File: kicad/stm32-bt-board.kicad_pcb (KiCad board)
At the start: 4 copper layers, 55 x 35.2 mm, 54 parts, among them J1 1909763-1, J2 2171790001, J3 Conn_ARM_SWD_TagConnect_TC2030, J4 S4B-PH-K-S(LF)(SN), Q1 S9013-E, SW1 B3U-1000P, SW2 B3U-1000P, U1 MIC5365-3.3YD5, U2 USBLC6-2SC6, U3 USBLC6-2SC6, U4 STM32WB55CEU6, X1 32MHz, X2 32kHz768

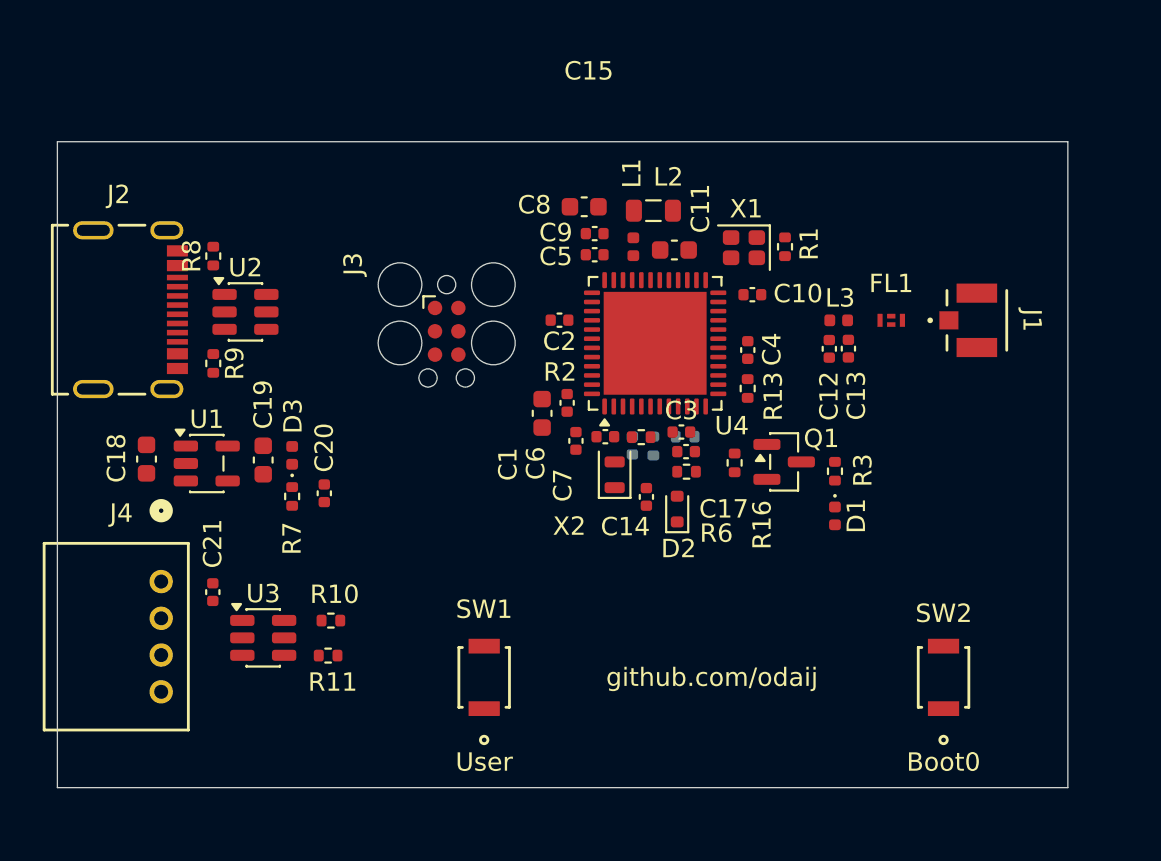
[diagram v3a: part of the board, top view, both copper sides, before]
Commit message: feat(layout & footprints): adjust layout and enhance custom footprints
adjust decoupling capacitors' positions and almost everything else
use rounded rectangular pads for all custom footprints, and update the pcb layout accordingly
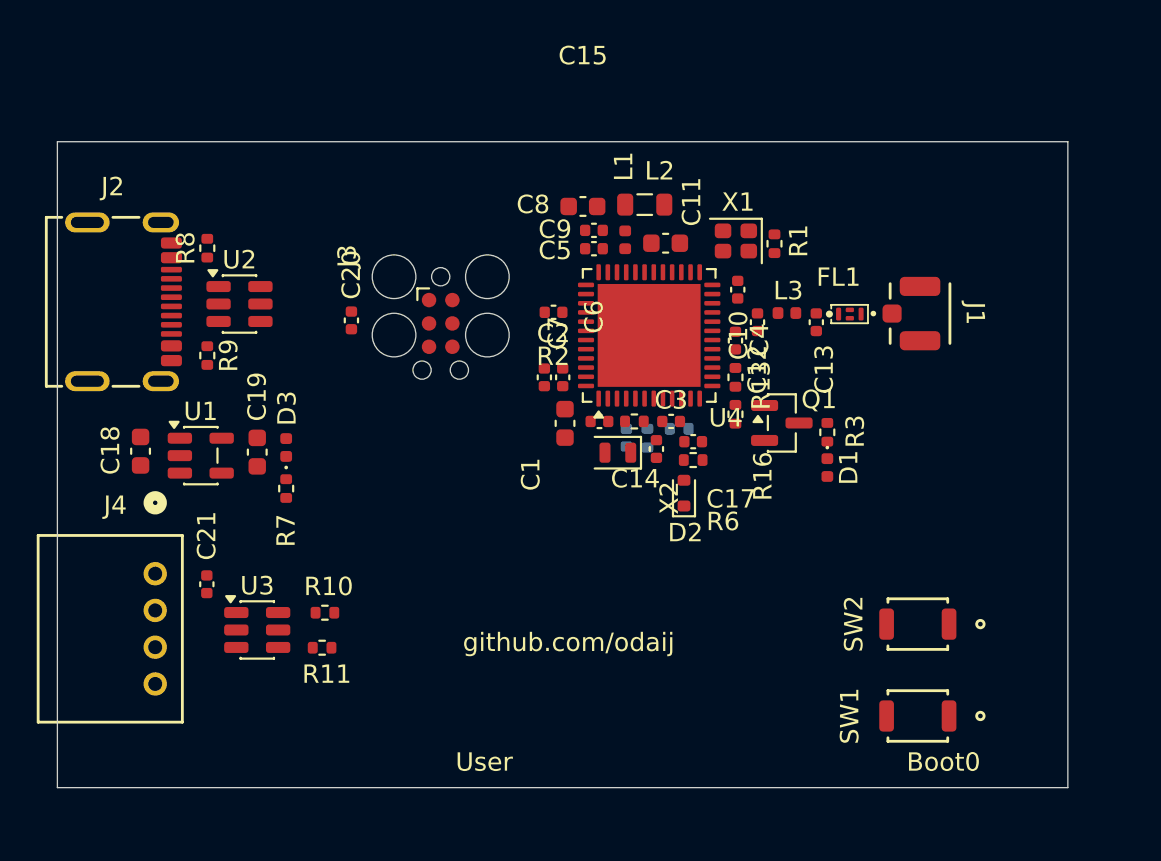
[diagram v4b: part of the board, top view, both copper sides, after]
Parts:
- moved SW1 23.7 mm to (169.0, 118.0), turned to 180 degrees
- moved C20 9.52 mm to (138.2, 96.5)
- moved C12 4.17 mm to (160.3, 96.6)
- moved C7 3.86 mm to (148.7, 99.6), turned to 90 degrees
- moved SW2 3.22 mm to (169.0, 113.0), turned to 180 degrees
- moved J1 3.11 mm to (169.1, 96.1)
- moved FL1 2.89 mm to (164.7, 96.1)
- moved L3 2.85 mm to (161.9, 96.1)
- moved C14 2.66 mm to (154.8, 103.5)
- moved D1 2.66 mm to (164.1, 104.5)
- moved R16 2.64 mm to (159.1, 101.6)
- moved C13 2.26 mm to (163.5, 96.6)
- moved R3 2.16 mm to (164.1, 102.6)
- moved Q1 2.12 mm to (161.6, 102.1)
- moved C6 1.41 mm to (149.7, 99.6), turned to 90 degrees
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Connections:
- net Net-(R1-Pad2) renamed /Microcontroller/Crystals/OSC_HSE_OUT_R

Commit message: i am in a hurry
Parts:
- moved C18 9.24 mm to (135.1, 99.7), turned to 180 degrees
- moved D3 5.75 mm to (135.6, 109.0), turned to 0 degrees
- moved R9 5.09 mm to (127.2, 102.4), turned to 180 degrees
- moved U1 5.07 mm to (134.9, 102.6), turned to -90 degrees
- moved R7 3.63 mm to (133.4, 109.0), turned to 180 degrees
- moved R8 3.49 mm to (127.2, 91.0), turned to 180 degrees
- moved U2 2.93 mm to (134.9, 96.4)
- moved C19 2.79 mm to (135.1, 105.5), turned to 180 degrees
- moved J2 2.12 mm to (126.8, 96.7)
- moved C14 1.13 mm to (154.7, 104.6)
- moved R1 1.03 mm to (162.1, 91.8)
- moved X1 1.03 mm to (160.0, 91.7)
- moved C16 0.97 mm to (154.1, 103.2)
- moved R5 0.88 mm to (155.1, 103.2)
- moved C15 0.73 mm to (151.6, 102.7)
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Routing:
- net /Microcontroller/BOOT0: track 0.00 -> 4.62 mm, vias 0 -> 1
- net /Microcontroller/OSC_LSE_IN: track 0.00 -> 3.76 mm
- net /Microcontroller/Crystals/OSC_LSE_OUT_R: track 0.00 -> 3.44 mm
- net /Microcontroller/OSC_LSE_OUT: track 0.00 -> 2.13 mm

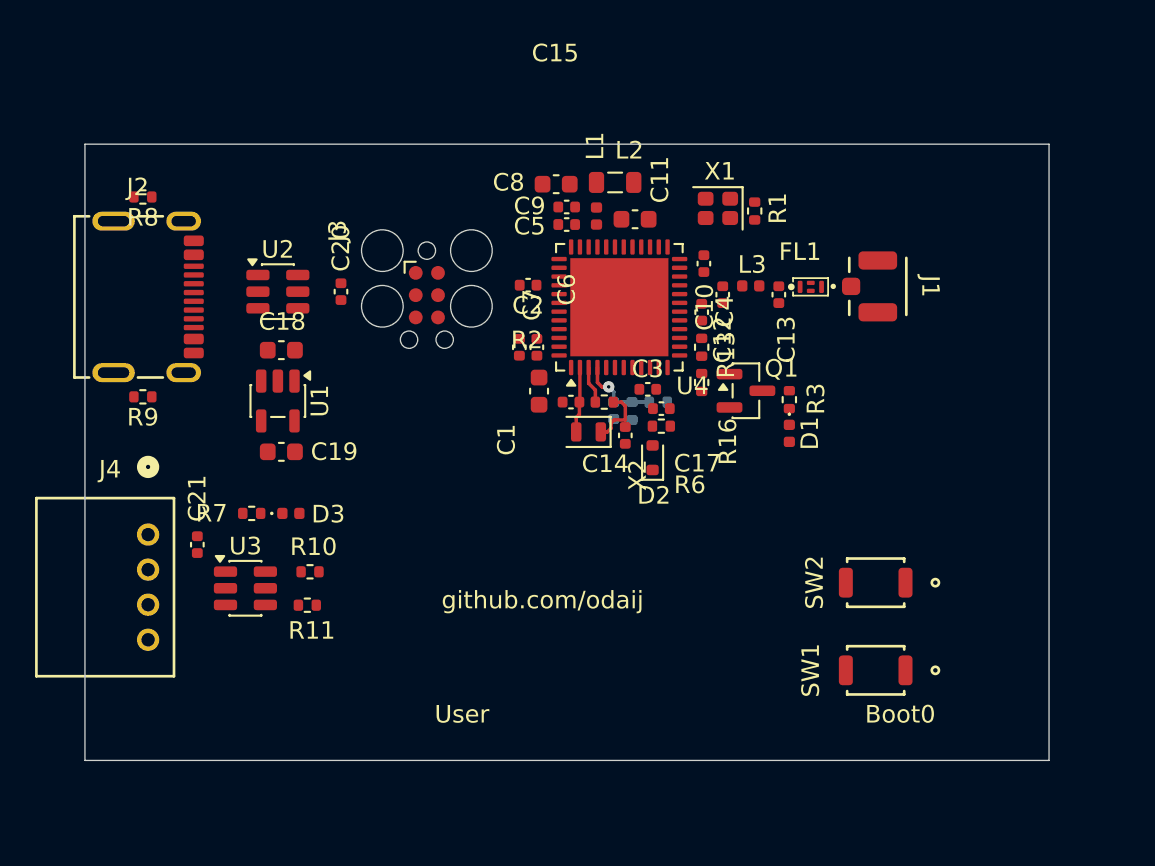
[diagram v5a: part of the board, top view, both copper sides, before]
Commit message: feat(layout): add vias, inner layer fills, and fully/partially route rf, usb, swd, uart, and power
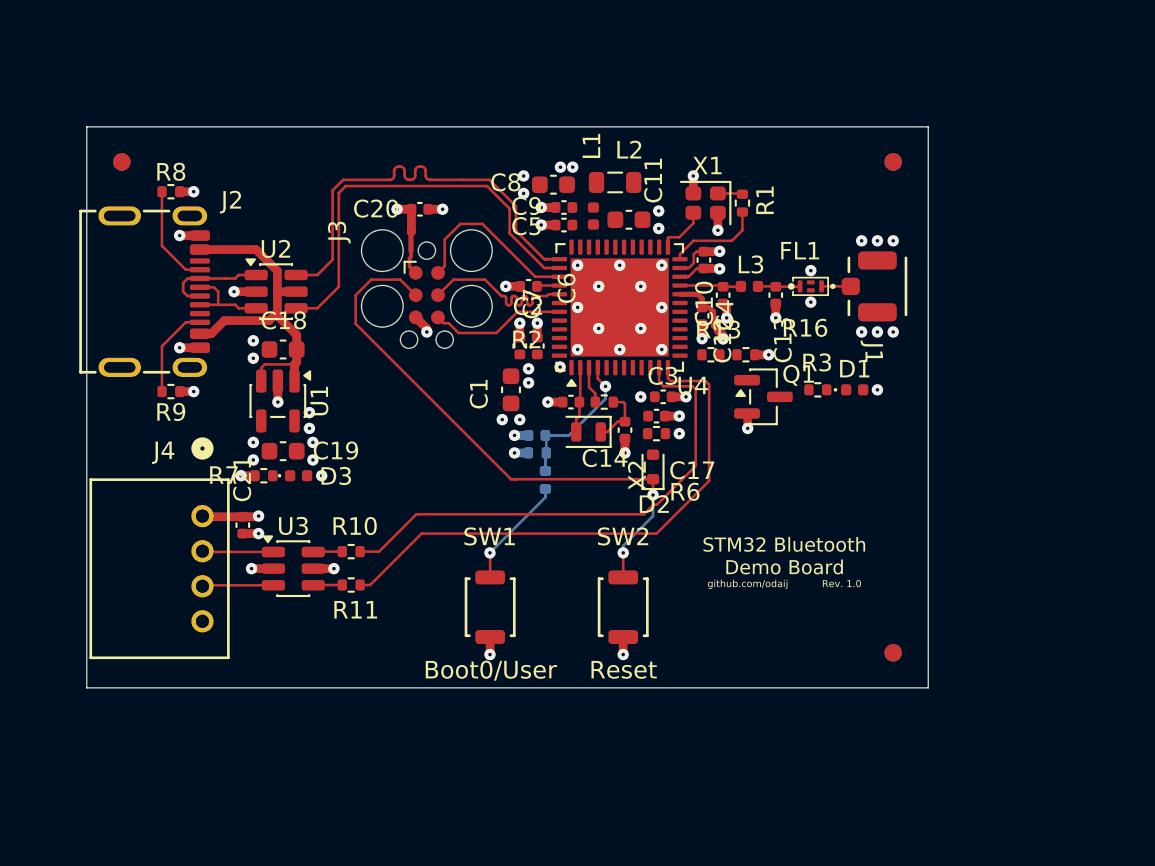
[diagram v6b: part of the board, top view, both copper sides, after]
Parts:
- added FID1: Fiducial, Fiducial:Fiducial_1mm_Mask2mm, F.Cu at (126.0, 89.0)
- added FID2: Fiducial, Fiducial:Fiducial_1mm_Mask2mm, F.Cu at (170.0, 89.0)
- added FID3: Fiducial, Fiducial:Fiducial_1mm_Mask2mm, F.Cu at (170.0, 117.0)
- added FID4: Fiducial, Fiducial:Fiducial_1mm_Mask2mm, B.Cu at (170.0, 89.0)
- added FID5: Fiducial, Fiducial:Fiducial_1mm_Mask2mm, B.Cu at (170.0, 117.0)
- added FID6: Fiducial, Fiducial:Fiducial_1mm_Mask2mm, B.Cu at (126.0, 89.0)
- moved SW1 22.3 mm to (147.0, 114.4), turned to 90 degrees
- moved SW2 14.5 mm to (154.6, 114.4), turned to 90 degrees
- moved R4 7.82 mm to (150.2, 107.1), turned to 90 degrees
- moved C20 6.51 mm to (143.0, 91.7), turned to 0 degrees
- moved R5 5.91 mm to (149.7, 105.6), turned to 180 degrees
- moved C16 4.60 mm to (149.7, 104.6), turned to 180 degrees
- moved D1 4.48 mm to (167.8, 102.0), turned to 0 degrees
- moved J4 3.27 mm to (130.6, 109.2)
- moved R16 2.98 mm to (161.6, 100.0), turned to 180 degrees
- moved U3 2.95 mm to (135.8, 112.2)
- moved C21 2.82 mm to (132.9, 109.7)
- moved R11 2.75 mm to (139.1, 113.1)
- moved R10 2.62 mm to (139.1, 111.2)
- moved R7 2.26 mm to (134.1, 106.9)
- moved D3 2.19 mm to (136.1, 106.9)
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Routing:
- net NRST_IN: track 0.00 -> 32.9 mm, vias 0 -> 2
- net /UART_MCU_RX: track 0.00 -> 31.0 mm
- net GND: track 0.00 -> 29.9 mm, vias 0 -> 61
- net /UART_MCU_TX: track 0.00 -> 28.6 mm
- net /USB_D-: track 0.00 -> 24.5 mm
- net /USB_D+: track 0.00 -> 23.8 mm
- net +5V: track 0.00 -> 20.4 mm
- net +3V3: track 0.00 -> 18.7 mm, vias 0 -> 19
- net /SWD_SWDIO: track 0.00 -> 10.2 mm
- net /SWD_SWCLK: track 0.00 -> 10.2 mm
- net /SWD_SWO: track 0.00 -> 7.80 mm
- net Net-(R4-Pad1): track 0.00 -> 6.36 mm, vias 0 -> 1
- net /Connectors/USB Type C/USB_CON_D-: track 0.00 -> 5.91 mm
- net /Connectors/USB Type C/USB_CON_CC1: track 0.00 -> 5.82 mm
- net /Microcontroller/OSC_HSE_OUT: track 0.00 -> 5.45 mm
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- added copper zone on In1.Cu, net GND
- added copper zone on In2.Cu, net GND
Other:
- board size 55 x 35.2 mm -> 48 x 32 mm
- board text added: "Boot0/User"
- board text added: "Reset"
- board text added: "STM32 Bluetooth Demo Board"
- board text added: "github.com/odaij Rev. 1.0"
- board text removed: "Boot0"
- board text removed: "User"
- board text removed: "github.com/odaij"

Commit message: feat(layout): big update
refine layout
add missing vias
complete routing
remove skew between USB_D+ and USB_D-
remove skew between SWD_SWCLK and SWD_SWDIO
add stitching vias
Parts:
- moved FID3 1.00 mm to (170.0, 118.0)
- moved FID5 1.00 mm to (170.0, 118.0)
- moved C2 0.51 mm to (148.7, 96.0)
- moved FL1 0.40 mm to (165.1, 96.1)
- moved J1 0.40 mm to (169.5, 96.1)
- moved C12 0.40 mm to (160.7, 96.6)
- moved C13 0.40 mm to (163.7, 96.6)
- moved L3 0.40 mm to (162.2, 96.1)
- moved C20 0.12 mm to (142.9, 91.7)
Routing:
- net /Microcontroller/NRST: track 0.00 -> 5.79 mm
- net +3V3: track 18.7 -> 23.7 mm, vias 19 -> 20
- net GND: track 29.9 -> 33.3 mm, vias 61 -> 193
- net Net-(Q1-B): track 0.00 -> 2.81 mm
- net /Microcontroller/USER_LED: track 0.00 -> 2.50 mm
- net Net-(Q1-C): track 0.00 -> 1.82 mm
- net /Microcontroller/Micellaneous/USER_LED_CATHODE: track 0.00 -> 1.10 mm
- net /LDO/3V3_LED_CATHODE: track 0.00 -> 0.99 mm
- net /USB_D-: track 24.5 -> 23.6 mm
- net /SWD_SWDIO: track 10.2 -> 10.8 mm
- net /SWD_SWCLK: track 10.2 -> 10.7 mm
- added copper zone on B.Cu, net +3V3
- added copper zone on F.Cu, net +3V3
- added copper zone on F.Cu, net /Microcontroller/SMPS/SMPS_LXL
- added copper zone on F.Cu, net /Microcontroller/SMPS_FB
- added copper zone on F.Cu, net /Microcontroller/SMPS_LX
- added copper zone on F.Cu, net GND
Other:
- board size 48 x 32 mm -> 48 x 33 mm
- board text added: "Stitching Via Spacing Equation Spacing in mm = c/20/sqrt(dielectric constant)/(highest freq content on the board) *1e3 in our case: Spacing in mm = c/20/sqrt(4.1)/2.4e9 * 1e3 = 3.08 mm for the dielectric you should use the effective value (air + prepreg); as we are routing the 2.4 GHz signal on the outer layer. but this will do for now"

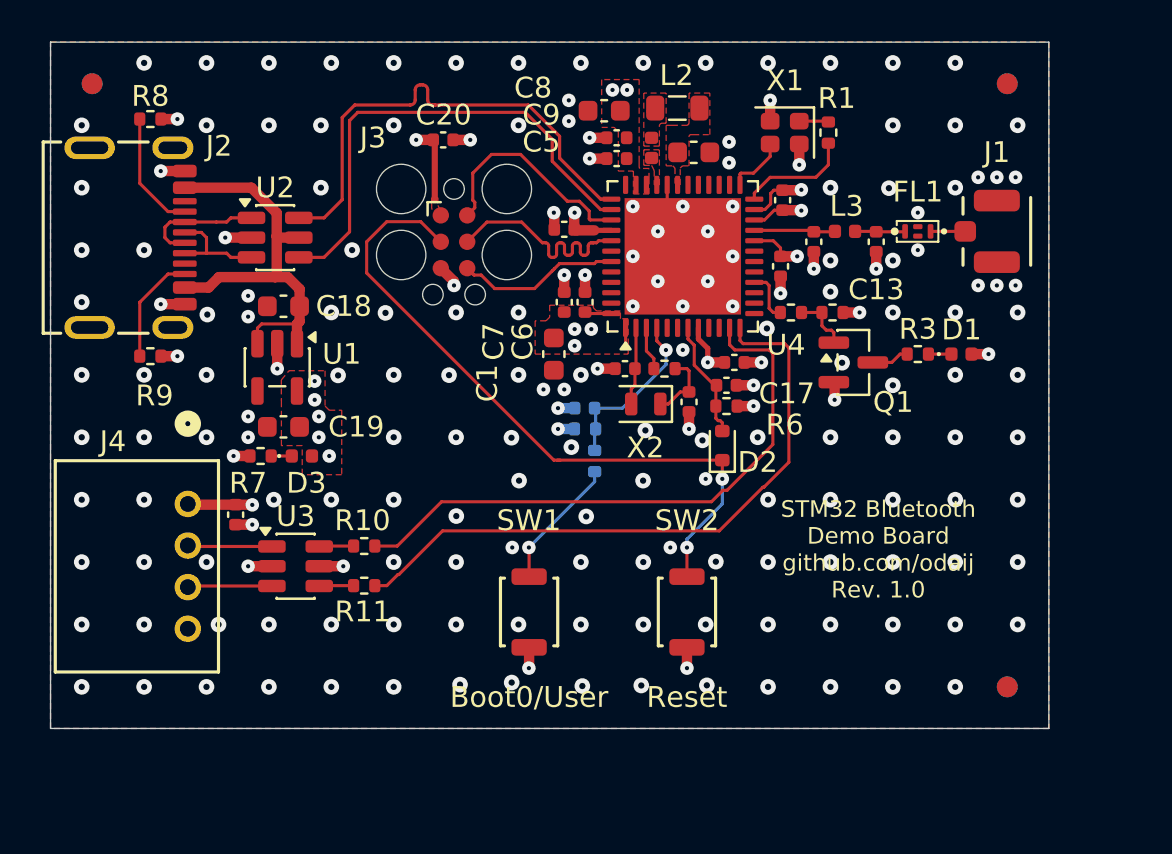
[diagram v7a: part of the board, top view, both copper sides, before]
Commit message: feat(layout): refine layout
remove unused pads and vias using the built-in utility - keeping the outside pads there even if unused
update D2 footprint to add a polarity dot of radius 0.2mm
add guiding silkscreen for the connectors; RF, SWD, and UART
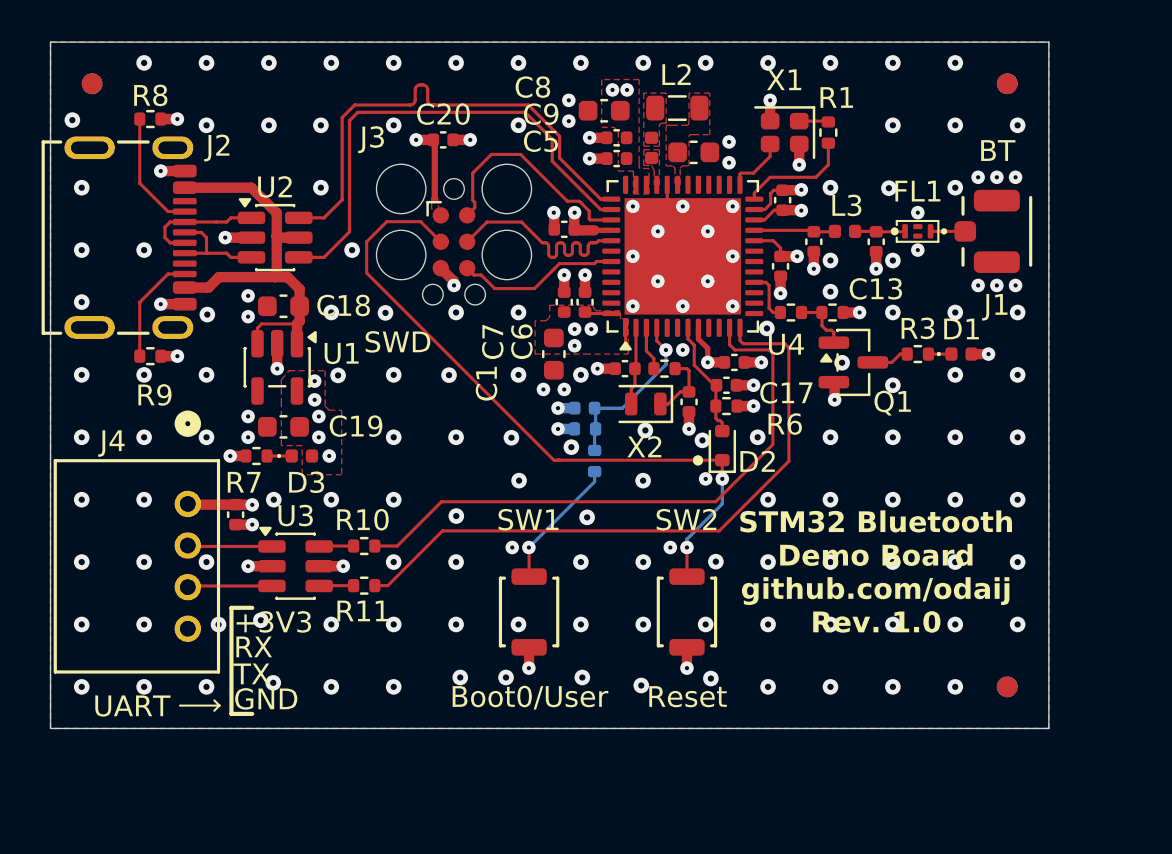
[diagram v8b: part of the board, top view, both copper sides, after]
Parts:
- moved R7 0.20 mm to (133.9, 106.9)
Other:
- board text added: "+3V3"
- board text added: "BT"
- board text added: "GND"
- board text added: "RX"
- board text added: "SWD"
- board text added: "TX"
- board text added: "UART"
